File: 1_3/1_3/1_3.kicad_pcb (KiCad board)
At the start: 2 copper layers, 137.5 x 93.4 mm, 52 parts, among them SW1 SW_SPST, SW10 SW_SPST, SW11 SW_SPST, SW12 SW_SPST, SW13 SW_SPST, SW14 SW_SPST, SW15 SW_SPST, SW16 SW_SPST, SW17 SW_SPST, SW18 SW_SPST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

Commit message: 1_3
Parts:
- moved D13 9.10 mm to (84.5, 98.8)
- moved D2 9.10 mm to (103.7, 77.3)
- moved D7 9.10 mm to (84.3, 81.1)
- moved D1 9.10 mm to (84.5, 77.3)
- moved D14 9.10 mm to (103.5, 98.7)
- moved D8 9.10 mm to (103.6, 81.2)
- moved H1 9.10 mm to (94.0, 76.5)
- moved H2 9.10 mm to (94.0, 95.5)
- moved SW1 9.10 mm to (84.5, 67.0)
- moved SW13 9.10 mm to (84.5, 105.0)
- moved SW14 9.10 mm to (103.5, 105.0)
- moved SW2 9.10 mm to (103.5, 67.0)
- moved SW7 9.10 mm to (84.5, 86.0)
- moved SW8 9.10 mm to (103.5, 86.0)
- moved D10 2.00 mm to (141.5, 74.1)
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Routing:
- net C2: track 166.2 -> 172.1 mm
- net R2: track 196.2 -> 190.7 mm
- net R0: track 198.9 -> 193.6 mm
- net C0: track 225.4 -> 220.5 mm
- net C1: track 202.6 -> 199.9 mm
- net Net-(D16-A): track 18.9 -> 21.4 mm
- net R1: track 185.0 -> 183.0 mm
- net Net-(D11-A): track 19.5 -> 21.3 mm
- net Net-(D17-A): track 20.6 -> 19.2 mm
- net Net-(D10-A): track 18.9 -> 17.6 mm
- net Net-(D5-A): track 17.5 -> 16.6 mm
- net Net-(D18-A): track 21.7 -> 20.9 mm
- net C3: track 173.7 -> 174.5 mm
- net Net-(D4-A): track 15.7 -> 16.5 mm
- net Net-(BT1--): track 66.1 -> 66.7 mm
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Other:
- board size 137.5 x 93.4 mm -> 137.5 x 91.4 mm
- board text added: "Ergonaut One v1.3 by yumagulovrn"
- board text removed: "Ergonaut One A v1.3 by yumagulovrn"

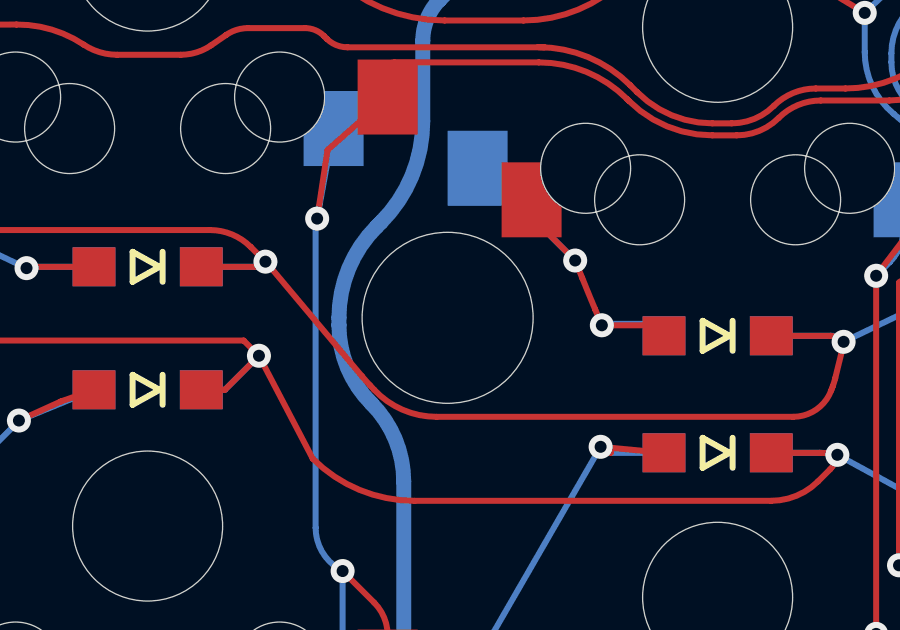
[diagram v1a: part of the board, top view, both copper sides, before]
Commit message: 1_3 mount hole update
step & gerbers update
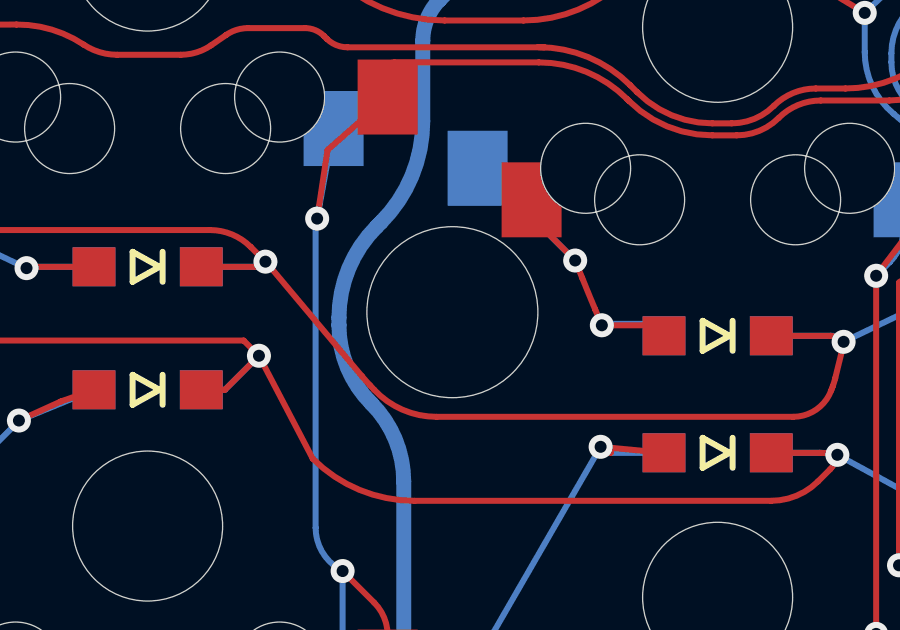
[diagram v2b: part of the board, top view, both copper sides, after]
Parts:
- moved H3 0.25 mm to (170.7, 74.1)

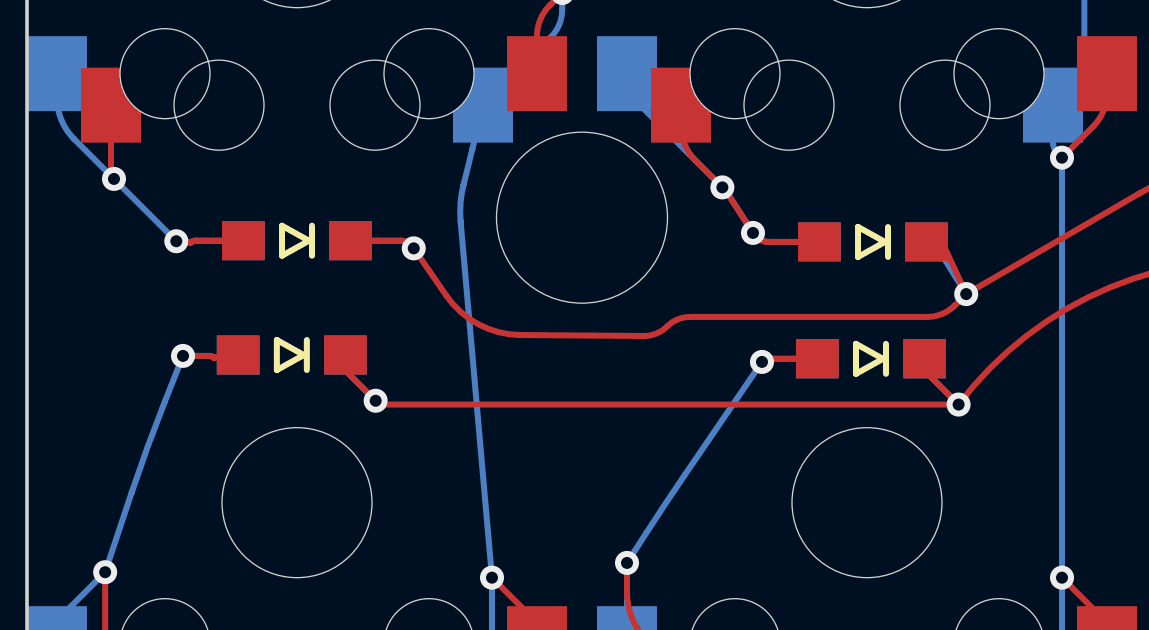
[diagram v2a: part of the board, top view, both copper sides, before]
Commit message: diode aligvent
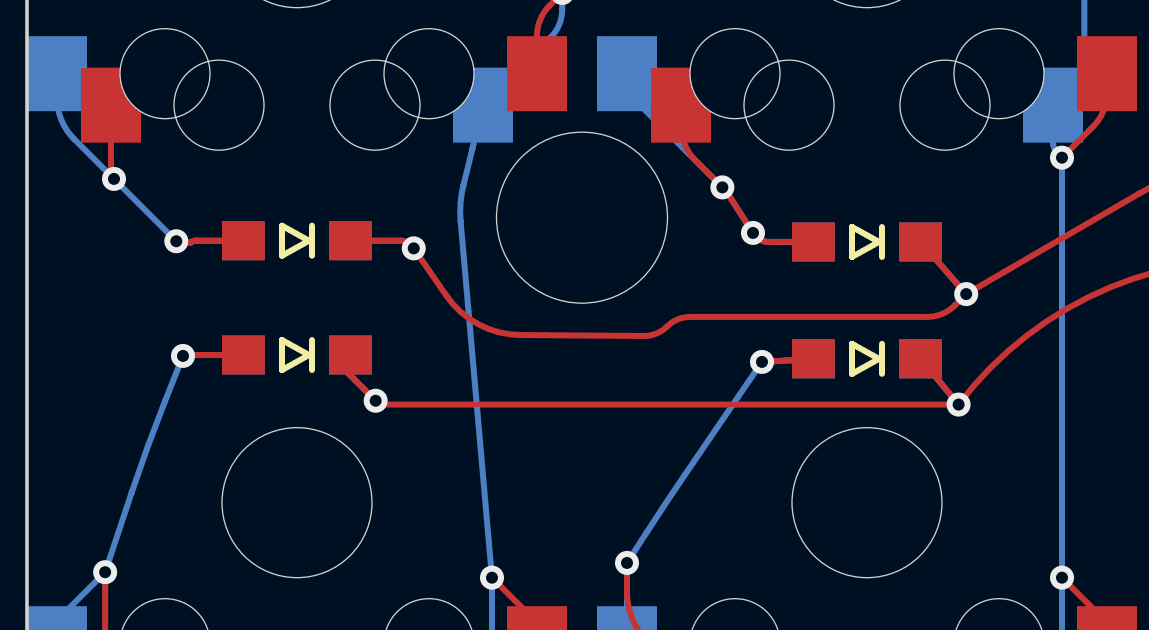
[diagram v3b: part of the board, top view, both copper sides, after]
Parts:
- moved D2 0.20 mm to (103.5, 77.3)
- moved D7 0.17 mm to (84.5, 81.1)
- moved D8 0.13 mm to (103.5, 81.2)
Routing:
- net Net-(D7-A): track 15.7 -> 16.7 mm
- net R1: track 183.0 -> 183.8 mm
- net Net-(D8-A): track 18.9 -> 19.5 mm

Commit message: 1_3 chk
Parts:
- moved H4 0.46 mm to (186.2, 116.0)
- moved D21 0.33 mm to (194.6, 125.1)
- moved H3 0.25 mm to (170.5, 74.3)
- moved H2 0.21 mm to (94.0, 95.7)
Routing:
- net R3: track 128.7 -> 128.1 mm
